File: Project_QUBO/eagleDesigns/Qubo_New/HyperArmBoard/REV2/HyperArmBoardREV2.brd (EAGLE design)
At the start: 96.8 x 88.9 mm, 16 parts, among them U1 BME280

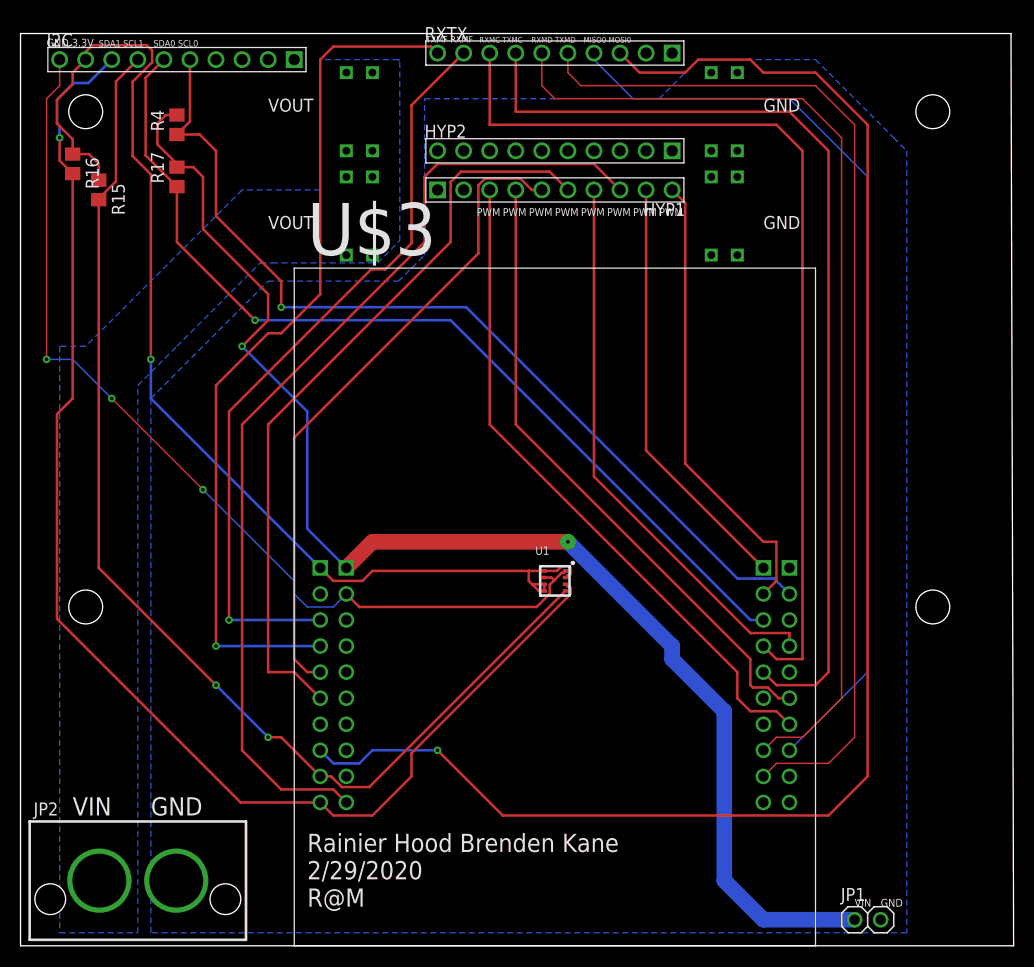
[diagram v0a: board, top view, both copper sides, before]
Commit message: made hyperarmboard
made newboard thatcombindes the hypertonics and arm board
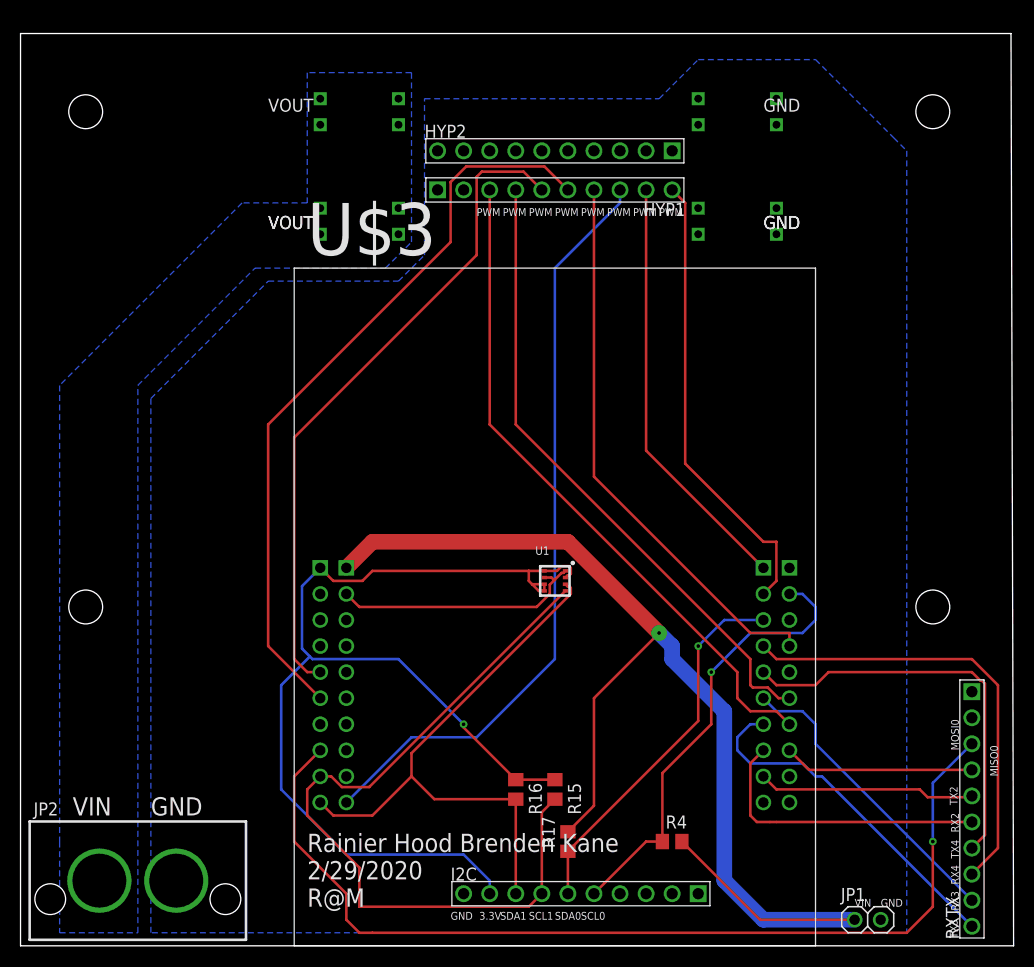
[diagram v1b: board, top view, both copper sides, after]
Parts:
- moved I2C 90.3 mm to (54.6, 5.08)
- moved R4 84.9 mm to (63.5, 10.2), turned to 0 degrees
- moved RXTX 84.1 mm to (92.7, 13.3), turned to 90 degrees
- moved R17 75.1 mm to (53.3, 10.2)
- moved R16 74.7 mm to (48.3, 15.2)
- moved R15 73.4 mm to (52.1, 15.2)
- moved U$6 1.37 mm to (69.8, 70.6), turned to 90 degrees
- moved U$7 1.27 mm to (69.8, 81.3), turned to 90 degrees
- moved U$5 0.51 mm to (33.0, 70.6), turned to 90 degrees
- turned U$4 to 270 degrees
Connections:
- net RX_MF: no longer RXTX.P$9
- net RX_SF: now also RXTX.P$9
- net TX_MF: no longer RXTX.P$10
- net TX_SF: now also RXTX.P$10
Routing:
- net TX_MF: track 84.5 -> 0.00 mm, vias 1 -> 0
- net TX_MD: track 102.1 -> 21.2 mm
- net RX_MF: track 74.4 -> 0.00 mm, vias 1 -> 0
- net MISO_0: track 91.1 -> 18.6 mm
- net SDA_1: track 128.3 -> 56.8 mm, vias 1 -> 0
- net DGND: track 95.1 -> 24.9 mm, vias 3 -> 0
- net RX_MD: track 98.8 -> 28.7 mm
- net TX_MC: track 96.0 -> 39.7 mm
- net SDA_0: track 92.2 -> 36.8 mm
- net MOSI_0: track 150.2 -> 95.8 mm
- net RX_MC: track 92.4 -> 43.9 mm
- net SCL_0: track 91.3 -> 43.9 mm
- net SCL_1: track 113.3 -> 75.6 mm, vias 2 -> 0
- net TX_SF: track 0.00 -> 34.3 mm
- net RX_SF: track 0.00 -> 29.6 mm
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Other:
- board text added: "3.3V"
- board text added: "MISO0"
- board text added: "MOSI0"
- board text added: "RX2"
- board text added: "RX3"
- board text added: "RX4"
- board text added: "SCL0"
- board text added: "SCL1"
- board text added: "SDA0"
- board text added: "SDA1"
- board text added: "TX2"
- board text added: "TX3"
- board text added: "TX4"
- board text removed: "GND 3.3V"
- board text removed: "MISO0 MOSI0"
- board text removed: "RXMC TXMC"
- board text removed: "RXMD TXMD"
- board text removed: "SDA0 SCL0"
- board text removed: "SDA1 SCL1"
- board text removed: "TXMF RXMF"
